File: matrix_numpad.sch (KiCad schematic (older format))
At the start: 34 parts

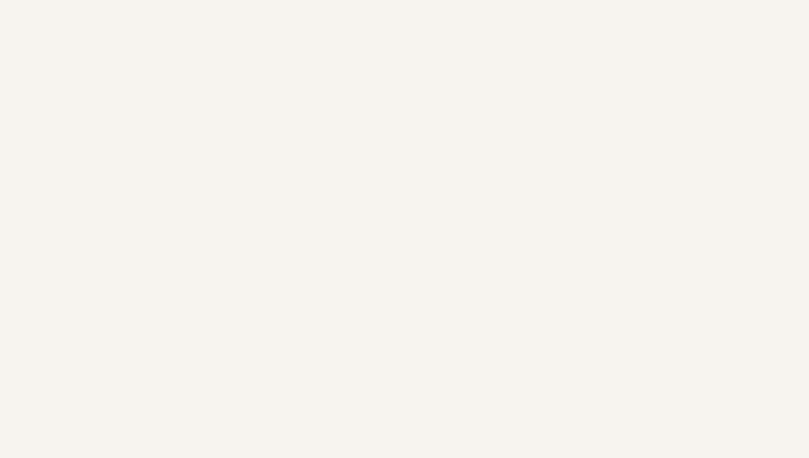
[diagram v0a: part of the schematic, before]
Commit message: Move board connectors to separate sheets, create breakout board for testing halves
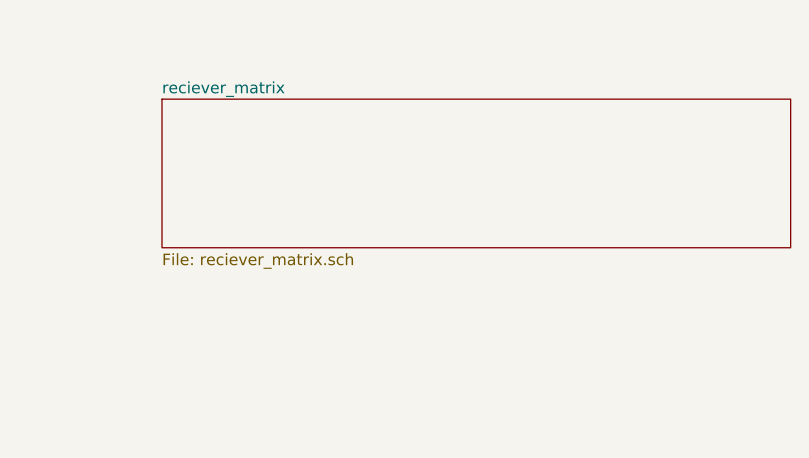
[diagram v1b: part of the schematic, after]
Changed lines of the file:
@@
 $Descr A2 23386 16535
 encoding utf-8
-Sheet 2 2
+Sheet 2 3
 Title ""
 Date ""
@@
 Wire Wire Line
 	2650 6000 2650 6100
+$Sheet
+S 13550 1950 2750 650
+U 5FF9299E
+F0 "reciever_matrix" 50
+F1 "reciever_matrix.sch" 50
+$EndSheet
 $EndSCHEMATC

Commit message: Layout and route numpad matrix
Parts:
- added A1: SSD1306_I2C_MODULE, Gigahawk:SSD1306_MODULE_128x32, symbol gigahawk:SSD1306_I2C_MODULE
- added C1, C3: 1u, Capacitor_SMD:C_0805_2012Metric_Pad1.15x1.40mm_HandSolder, symbol Device:C
- added C2, C4: 0.1u, Capacitor_SMD:C_0805_2012Metric_Pad1.15x1.40mm_HandSolder, symbol Device:C
- added D_ROT_0: D, keyboard_parts:D_SOD123_axial, symbol Device:D
- added R1, R12, R2: 20k, Resistor_SMD:R_0805_2012Metric_Pad1.15x1.40mm_HandSolder, symbol Device:R
- added R10, R11, R8, R9: DNI, Resistor_SMD:R_0805_2012Metric_Pad1.15x1.40mm_HandSolder, symbol Device:R
- added R3, R4, R5, R6, R7: 0R, Resistor_SMD:R_0805_2012Metric_Pad1.15x1.40mm_HandSolder, symbol Device:R
- added SW1: Rotary_Encoder_Switch, Gigahawk:482016514001, symbol Device:Rotary_Encoder_Switch
- added U1: MCP23017_SS, Package_SO:SSOP-28_5.3x10.2mm_P0.65mm, symbol Interface_Expansion:MCP23017_SS
- added U2: IS31FL3731-SA, Package_SO:SSOP-28_5.3x10.2mm_P0.65mm, symbol Driver_LED:IS31FL3731-SA
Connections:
- net col3 is gone; now on net ROT_S2: K_+_0.1, K_MINUS_0.1
- net col0: now also R4.2, R8.2
- net col1: now also R5.2, R9.2
- net col2: now also R10.2, R6.2
- net CA2: now reaches K_5_0.3 (A)
- net CA2: now also K_+_0.4 (K), K_DEL_0.3 (A), K_DOWN_0.3 (A), K_HOME_0.4 (K), K_NUM_LOCK_0.3 (A), K_PGUP_0.4 (K), K_UP_0.4 (K), U2.22 (CA2)
- net CA3: now reaches K_5_0.4 (K)
- net CA3: now also K_LEFT_0.4 (K), K_PGDN_0.3 (A), K_RIGHT_0.4 (K), K_SLASH_0.3 (A), K_UP_0.3 (A), U2.23 (CA3)
- net CA5: now reaches K_+_0.3 (A)
- net CA5: now also K_DEL_0.4 (K), K_ENTER_0.3 (A), K_INS_0.4 (K), K_MINUS_0.3 (A), U2.25 (CA5)
- net CA4: now reaches K_ENTER_0.4 (K)
- net CA4: now also K_*_0.3 (A), K_DOWN_0.4 (K), K_END_0.4 (K), K_PGDN_0.4 (K), K_PGUP_0.3 (A), K_RIGHT_0.3 (A), U2.24 (CA4)
- net CA1: now reaches K_HOME_0.3 (A)
- net CA1: now also K_*_0.4 (K), K_END_0.3 (A), K_INS_0.3 (A), K_LEFT_0.3 (A), K_MINUS_0.4 (K), K_NUM_LOCK_0.4 (K), K_SLASH_0.4 (K), U2.21 (CA1)
- net ROT_S2: now reaches K_ENTER_0.1
- net ROT_S2: now also R11.2, R7.2, SW1.S1
- net row0 renamed PD0
- net row1 renamed PD1
- net row2 renamed PD5
- net row3 renamed PD6
- net row4 renamed PD7
- net PD7: now also D_ROT_0.1 (K)
- new net: R3.2, U1.9 (VDD)
- new net: R12.1, U2.6 (R_EXT)
- new net +5V: A1.2 (VCC), C1.1, C2.1, C3.1, C4.1, R1.1, R2.2, R3.1, U1.18 (~RESET~), U2.2 (VCC), U2.3 (~SDB)
- new net GND: A1.1 (GND), C1.2, C2.2, C3.2, C4.2, R12.2, SW1.C, U1.10 (VSS), U1.15 (A0), U1.16 (A1), U1.17 (A2), U2.18 (AD), U2.5 (GND)
- new net GPA0: R4.1, U1.21 (GPA0)
- new net GPA1: R5.1, U1.22 (GPA1)
- new net GPA2: R6.1, U1.23 (GPA2)
- new net GPA3: R7.1, U1.24 (GPA3)
- new net PB0: R8.1
- new net PB1: R9.1
- new net PB2: R10.1
- new net PC2: R11.1, R2.1, SW1.B
- new net PC3: R1.2, SW1.A
- new net ROT_S1: D_ROT_0.2 (A), SW1.S2
- new net SCL: A1.3 (SCL), U1.12 (SCK), U2.20 (SCL)
- new net SDA: A1.4 (SDA), U1.13 (SDA), U2.19 (SDA)
- no-connect marks 0 -> 16
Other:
- note added: "I2C Address 0x3C\nMODULE MUST BE 5V TOLERANT"

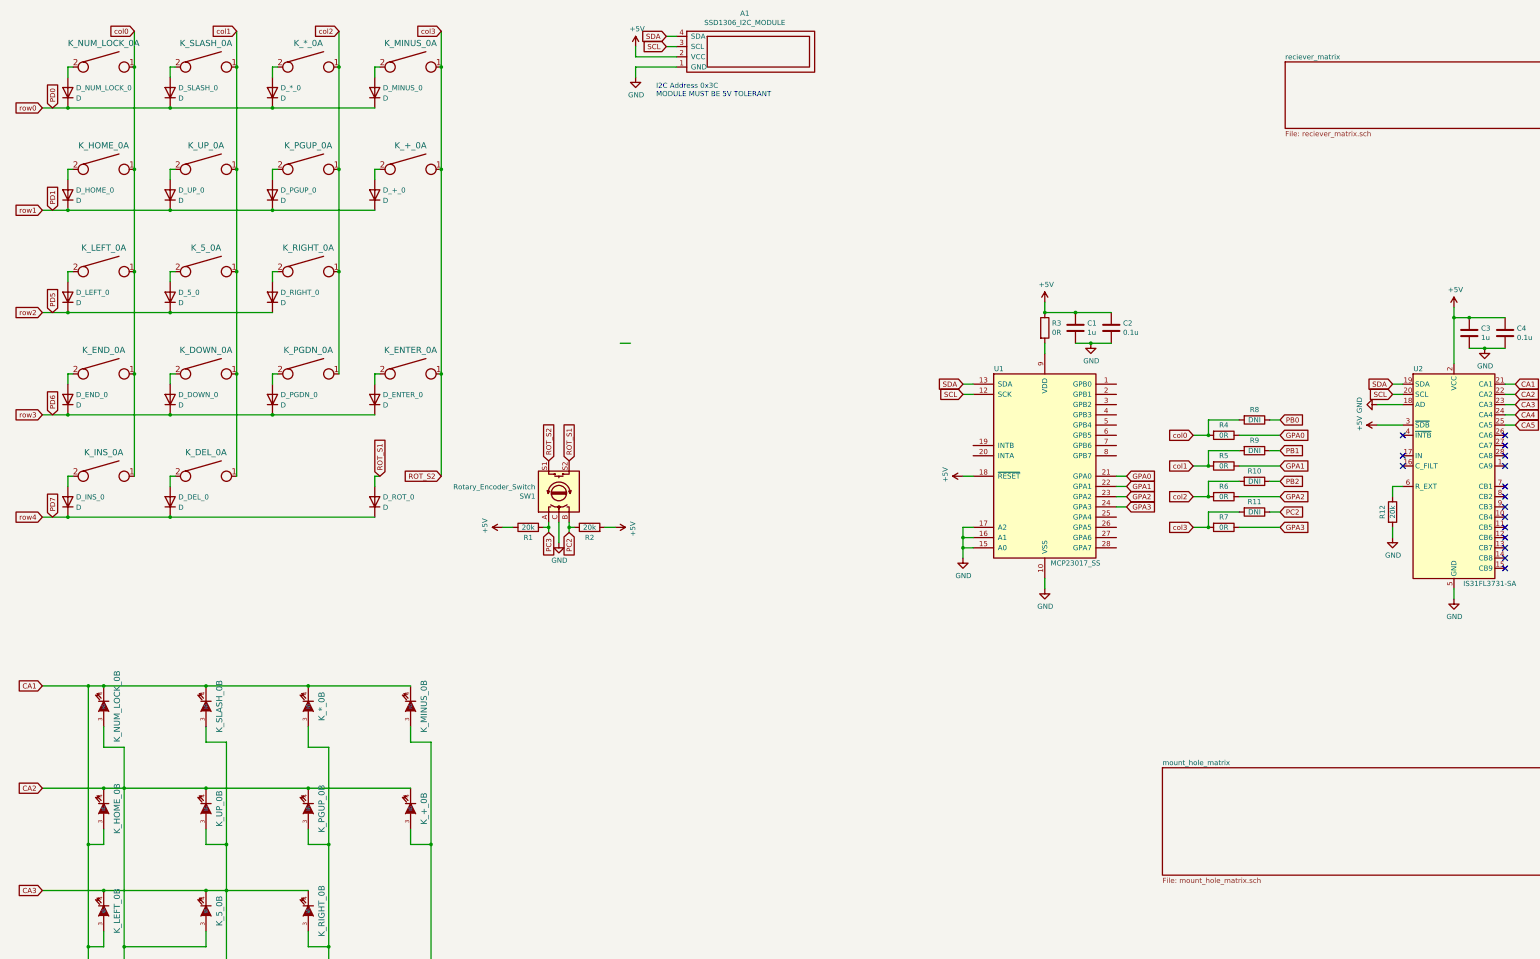
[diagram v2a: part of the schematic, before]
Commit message: Reroute matrix, redo schematics for feather compat
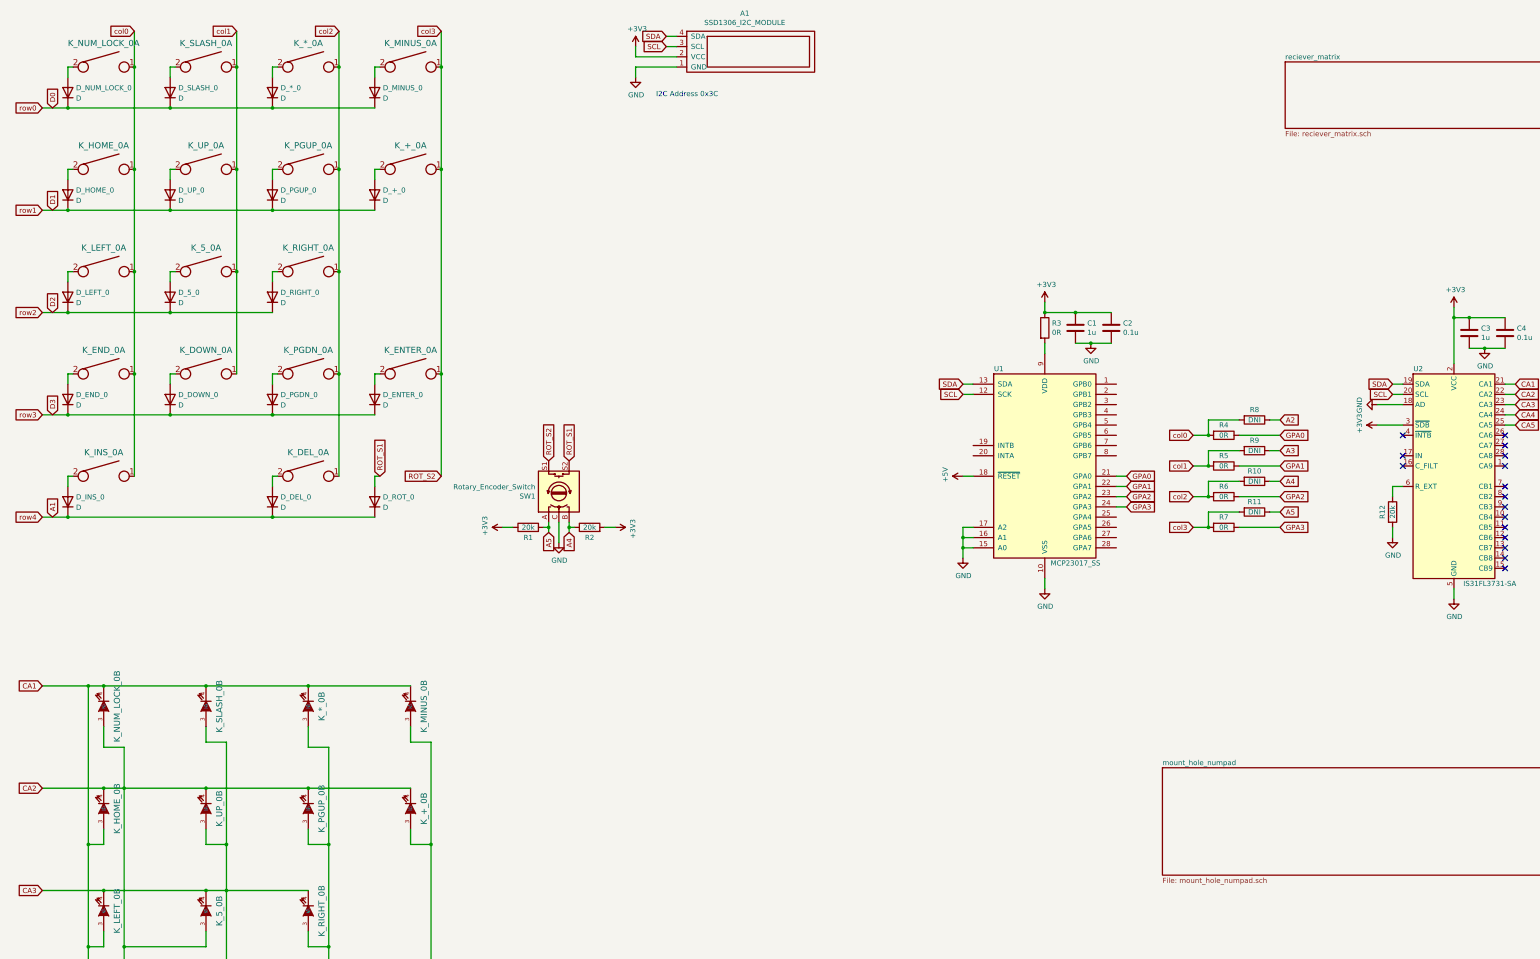
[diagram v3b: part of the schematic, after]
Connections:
- net +5V: no longer A1.2 (VCC), C1.1, C2.1, C3.1, C4.1, R1.1, R2.2, R3.1, U2.2 (VCC), U2.3 (~SDB)
- net col1: no longer K_DEL_0.1
- net col2: now also K_DEL_0.1
- net PB0 renamed A2
- net PB1 renamed A3
- net PB2 renamed A4
- net A4: now also R2.1, SW1.B
- removed net PC2: R11.1, R2.1, SW1.B
- net PC3 renamed A5
- net A5: now also R11.1
- net PD0 renamed D0
- net PD1 renamed D1
- net PD5 renamed D2
- net PD6 renamed D3
- net PD7 renamed A1
- new net +3V3: A1.2 (VCC), C1.1, C2.1, C3.1, C4.1, R1.1, R2.2, R3.1, U2.2 (VCC), U2.3 (~SDB)
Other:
- note added: "I2C Address 0x3C"
- note removed: "I2C Address 0x3C\nMODULE MUST BE 5V TOLERANT"
- moved on the sheet: D_DEL_0, K_DEL_0A
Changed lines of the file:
@@
 Wire Wire Line
 	2650 5000 2650 5100
-Connection ~ 3300 5000
 Connection ~ 2650 5400
 $Comp
@@
 L keyboard_parts:KEYSW K_DEL_0
 U 1 1 5FF5BFDA
-P 3000 6000
-F 0 "K_DEL_0" H 3000 6233 60  0000 C CNN
-F 1 "KEYSW" H 3000 5900 60  0001 C CNN
-F 2 "MX_Alps_Hybrid:MX-1U" H 3000 6000 60  0001 C CNN
-F 3 "" H 3000 6000 60  0000 C CNN
-	1    3000 6000
+P 4000 6000
+F 0 "K_DEL_0" H 4000 6233 60  0000 C CNN
+F 1 "KEYSW" H 4000 5900 60  0001 C CNN
+F 2 "MX_Alps_Hybrid:MX-1U" H 4000 6000 60  0001 C CNN
+F 3 "" H 4000 6000 60  0000 C CNN
+	1    4000 6000
 	1    0    0    -1
 $EndComp
@@
 L Device:D D_DEL_0
 U 1 1 CA2EE79A
-P 2650 6250
-F 0 "D_DEL_0" V 2696 6171 50  0000 R CNN
-F 1 "D" V 2595 6171 50  0000 R CNN
-F 2 "keyboard_parts:D_SOD123_axial" H 2650 6250 50  0001 C CNN
-F 3 "~" H 2650 6250 50  0001 C CNN
-	1    2650 6250
+P 3650 6250
+F 0 "D_DEL_0" V 3696 6171 50  0000 R CNN
+F 1 "D" V 3595 6171 50  0000 R CNN
+F 2 "keyboard_parts:D_SOD123_axial" H 3650 6250 50  0001 C CNN
+F 3 "~" H 3650 6250 50  0001 C CNN
+	1    3650 6250
 	0    -1   -1   0
 $EndComp
 Wire Wire Line
-	1650 6400 2650 6400
-Wire Wire Line
-	3300 5000 3300 6000
-Wire Wire Line
-	2700 6000 2650 6000
-Wire Wire Line
-	2650 6000 2650 6100
+	3700 6000 3650 6000
+Wire Wire Line
+	3650 6000 3650 6100
 $Sheet
 S 13550 1950 2750 650
@@
 Wire Wire Line
 	7500 1800 7600 1800
-$Comp
-L power:+5V #PWR?
-U 1 1 5FF9C11A
-P 7200 1800
-AR Path="/5FF53271/5FF9C11A" Ref="#PWR?"  Part="1"
-AR Path="/5FF53271/5FF7CBCC/5FF9C11A" Ref="#PWR?"  Part="1"
-AR Path="/5FF5604D/5FF9299E/5FF9C11A" Ref="#PWR?"  Part="1"
-AR Path="/5FF77C9D/5FF9C11A" Ref="#PWR?"  Part="1"
-AR Path="/5FF5604D/5FF9C11A" Ref="#PWR0101"  Part="1"
-F 0 "#PWR0101" H 7200 1650 50  0001 C CNN
-F 1 "+5V" H 7215 1973 50  0000 C CNN
-F 2 "" H 7200 1800 50  0001 C CNN
-F 3 "" H 7200 1800 50  0001 C CNN
-	1    7200 1800
-	1    0    0    -1
-$EndComp
 Wire Wire Line
 	7600 1900 7200 1900
@@
 	7200 2000 7200 2100
 Text Notes 7400 2300 0    50   ~ 0
-I2C Address 0x3C\nMODULE MUST BE 5V TOLERANT
-$Comp
-L power:+5V #PWR?
-U 1 1 5FFAD4E0
-P 11200 4300
-AR Path="/5FF53271/5FFAD4E0" Ref="#PWR?"  Part="1"
-AR Path="/5FF53271/5FF7CBCC/5FFAD4E0" Ref="#PWR?"  Part="1"
-AR Path="/5FF5604D/5FF9299E/5FFAD4E0" Ref="#PWR?"  Part="1"
-AR Path="/5FF77C9D/5FFAD4E0" Ref="#PWR?"  Part="1"
-AR Path="/5FF5604D/5FFAD4E0" Ref="#PWR0103"  Part="1"
-F 0 "#PWR0103" H 11200 4150 50  0001 C CNN
-F 1 "+5V" H 11215 4473 50  0000 C CNN
-F 2 "" H 11200 4300 50  0001 C CNN
-F 3 "" H 11200 4300 50  0001 C CNN
-	1    11200 4300
-	1    0    0    -1
-$EndComp
+I2C Address 0x3C
 Text GLabel 10400 5100 0    50   Input ~ 0
 SDA
@@
 	10400 6500 10400 6600
 Connection ~ 10400 6600
-Text GLabel 1500 2400 1    50   Input ~ 0
-PD0
 Text GLabel 1500 3400 1    50   Input ~ 0
-PD1
+D1
 Text GLabel 1500 4400 1    50   Input ~ 0
-PD5
+D2
 Text GLabel 1500 5400 1    50   Input ~ 0
-PD6
+D3
 Text GLabel 1500 6400 1    50   Input ~ 0
-PD7
+A1
 Text GLabel 12000 6000 2    50   Input ~ 0
 GPA0
@@
 col0
 Text GLabel 13500 5450 2    50   Input ~ 0
-PB0
+A2
 Text GLabel 13500 5750 2    50   Input ~ 0
-PB1
+A3
 Text GLabel 13500 6050 2    50   Input ~ 0
-PB2
+A4
 Text GLabel 13500 6350 2    50   Input ~ 0
-PC2
-Text GLabel 6350 6550 3    50   Input ~ 0
-PC3
-Wire Wire Line
-	7050 4700 7150 4700
+A5
 $Comp
 L Driver_LED:IS31FL3731-SA U2
@@
 F 3 "~" H 15350 4600 50  0001 C CNN
 	1    15350 4600
-	1    0    0    -1
-$EndComp
-$Comp
-L power:+5V #PWR?
-U 1 1 6005FFC4
-P 15200 4350
-AR Path="/5FF53271/6005FFC4" Ref="#PWR?"  Part="1"
-AR Path="/5FF53271/5FF7CBCC/6005FFC4" Ref="#PWR?"  Part="1"
-AR Path="/5FF5604D/5FF9299E/6005FFC4" Ref="#PWR?"  Part="1"
-AR Path="/5FF77C9D/6005FFC4" Ref="#PWR?"  Part="1"
-AR Path="/5FF5604D/6005FFC4" Ref="#PWR010"  Part="1"
-F 0 "#PWR010" H 15200 4200 50  0001 C CNN
-F 1 "+5V" H 15215 4523 50  0000 C CNN
-F 2 "" H 15200 4350 50  0001 C CNN
-F 3 "" H 15200 4350 50  0001 C CNN
-	1    15200 4350
 	1    0    0    -1
 $EndComp
@@
 NoConn ~ 15700 5800
 NoConn ~ 15700 5900
-$Comp
-L power:+5V #PWR?
-U 1 1 603D25FD
-P 14450 5500
-AR Path="/5FF53271/603D25FD" Ref="#PWR?"  Part="1"
-AR Path="/5FF53271/5FF7CBCC/603D25FD" Ref="#PWR?"  Part="1"
-AR Path="/5FF5604D/5FF9299E/603D25FD" Ref="#PWR?"  Part="1"
-AR Path="/5FF77C9D/603D25FD" Ref="#PWR?"  Part="1"
-AR Path="/5FF5604D/603D25FD" Ref="#PWR08"  Part="1"
-F 0 "#PWR08" H 14450 5350 50  0001 C CNN
-F 1 "+5V" H 14465 5673 50  0000 C CNN
-F 2 "" H 14450 5500 50  0001 C CNN
-F 3 "" H 14450 5500 50  0001 C CNN
-	1    14450 5500
-	0    -1   -1   0
-$EndComp
 Wire Wire Line
 	14700 5500 14450 5500
@@
 	0    -1   -1   0
 $EndComp
-Wire Wire Line
-	2650 6400 4650 6400
-Connection ~ 2650 6400
 Text GLabel 6550 5850 1    50   Input ~ 0
 ROT_S1
@@
 	5300 5000 5300 6000
 Connection ~ 5300 5000
-Text GLabel 6550 6550 3    50   Input ~ 0
-PC2
 $Comp
 L power:GND #PWR?
@@
 Wire Wire Line
 	6550 6500 6550 6550
-$Comp
-L power:+5V #PWR?
-U 1 1 604A5BAA
+Wire Wire Line
+	5900 6500 6000 6500
+Wire Wire Line
+	6900 6500 7000 6500
+$Comp
+L power:+3V3 #PWR0101
+U 1 1 60488DA6
+P 7200 1800
+F 0 "#PWR0101" H 7200 1650 50  0001 C CNN
+F 1 "+3V3" H 7215 1973 50  0000 C CNN
+F 2 "" H 7200 1800 50  0001 C CNN
+F 3 "" H 7200 1800 50  0001 C CNN
+	1    7200 1800
+	1    0    0    -1
+$EndComp
+Text GLabel 1500 2400 1    50   Input ~ 0
+D0
+Text GLabel 6350 6550 3    50   Input ~ 0
+A5
+Text GLabel 6550 6550 3    50   Input ~ 0
+A4
+$Sheet
+S 12350 8850 3750 1050
+U 5FFADEAF
+F0 "mount_hole_numpad" 50
+F1 "mount_hole_numpad.sch" 50
+$EndSheet
+$Comp
+L power:+3V3 #PWR0103
+U 1 1 6049B8FB
+P 7000 6500
+F 0 "#PWR0103" H 7000 6350 50  0001 C CNN
+F 1 "+3V3" H 7015 6673 50  0000 C CNN
+F 2 "" H 7000 6500 50  0001 C CNN
+F 3 "" H 7000 6500 50  0001 C CNN
+	1    7000 6500
+	0    1    1    0
+$EndComp
+$Comp
+L power:+3V3 #PWR0107
+U 1 1 604A934F
 P 5900 6500
-AR Path="/5FF53271/604A5BAA" Ref="#PWR?"  Part="1"
-AR Path="/5FF53271/5FF7CBCC/604A5BAA" Ref="#PWR?"  Part="1"
-AR Path="/5FF5604D/5FF9299E/604A5BAA" Ref="#PWR?"  Part="1"
-AR Path="/5FF77C9D/604A5BAA" Ref="#PWR?"  Part="1"
-AR Path="/5FF5604D/604A5BAA" Ref="#PWR03"  Part="1"
-F 0 "#PWR03" H 5900 6350 50  0001 C CNN
-F 1 "+5V" H 5915 6673 50  0000 C CNN
+F 0 "#PWR0107" H 5900 6350 50  0001 C CNN
+F 1 "+3V3" H 5915 6673 50  0000 C CNN
 F 2 "" H 5900 6500 50  0001 C CNN
 F 3 "" H 5900 6500 50  0001 C CNN
@@
 	0    -1   -1   0
 $EndComp
-Wire Wire Line
-	5900 6500 6000 6500
-$Comp
-L power:+5V #PWR?
-U 1 1 604B3C1E
-P 7000 6500
-AR Path="/5FF53271/604B3C1E" Ref="#PWR?"  Part="1"
-AR Path="/5FF53271/5FF7CBCC/604B3C1E" Ref="#PWR?"  Part="1"
-AR Path="/5FF5604D/5FF9299E/604B3C1E" Ref="#PWR?"  Part="1"
-AR Path="/5FF77C9D/604B3C1E" Ref="#PWR?"  Part="1"
-AR Path="/5FF5604D/604B3C1E" Ref="#PWR05"  Part="1"
-F 0 "#PWR05" H 7000 6350 50  0001 C CNN
-F 1 "+5V" H 7015 6673 50  0000 C CNN
-F 2 "" H 7000 6500 50  0001 C CNN
-F 3 "" H 7000 6500 50  0001 C CNN
-	1    7000 6500
-	0    1    1    0
-$EndComp
-Wire Wire Line
-	6900 6500 7000 6500
-$Sheet
-S 12350 8850 3750 1050
-U 5FFADEAF
-F0 "mount_hole_matrix" 50
-F1 "mount_hole_matrix.sch" 50
-$EndSheet
+$Comp
+L power:+3V3 #PWR0108
+U 1 1 604A96DA
+P 11200 4300
+F 0 "#PWR0108" H 11200 4150 50  0001 C CNN
+F 1 "+3V3" H 11215 4473 50  0000 C CNN
+F 2 "" H 11200 4300 50  0001 C CNN
+F 3 "" H 11200 4300 50  0001 C CNN
+	1    11200 4300
+	1    0    0    -1
+$EndComp
+$Comp
+L power:+3V3 #PWR0109
+U 1 1 604AA0CB
+P 15200 4350
+F 0 "#PWR0109" H 15200 4200 50  0001 C CNN
+F 1 "+3V3" H 15215 4523 50  0000 C CNN
+F 2 "" H 15200 4350 50  0001 C CNN
+F 3 "" H 15200 4350 50  0001 C CNN
+	1    15200 4350
+	1    0    0    -1
+$EndComp
+Connection ~ 3650 6400
+Wire Wire Line
+	3650 6400 4650 6400
+Wire Wire Line
+	1650 6400 3650 6400
+Wire Wire Line
+	4300 6000 4300 5000
+Connection ~ 4300 5000
+$Comp
+L power:+3V3 #PWR?
+U 1 1 604FDB56
+P 14450 5500
+F 0 "#PWR?" H 14450 5350 50  0001 C CNN
+F 1 "+3V3" H 14465 5673 50  0000 C CNN
+F 2 "" H 14450 5500 50  0001 C CNN
+F 3 "" H 14450 5500 50  0001 C CNN
+	1    14450 5500
+	0    -1   -1   0
+$EndComp
 $EndSCHEMATC
